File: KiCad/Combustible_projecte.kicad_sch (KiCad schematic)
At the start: 0 parts

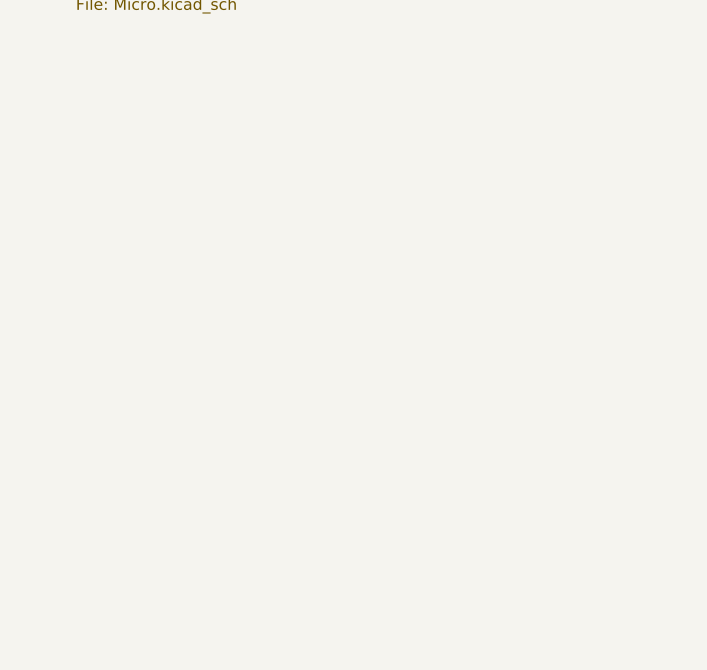
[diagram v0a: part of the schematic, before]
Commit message: Part de potencia acabada, concretar certs pins del micro
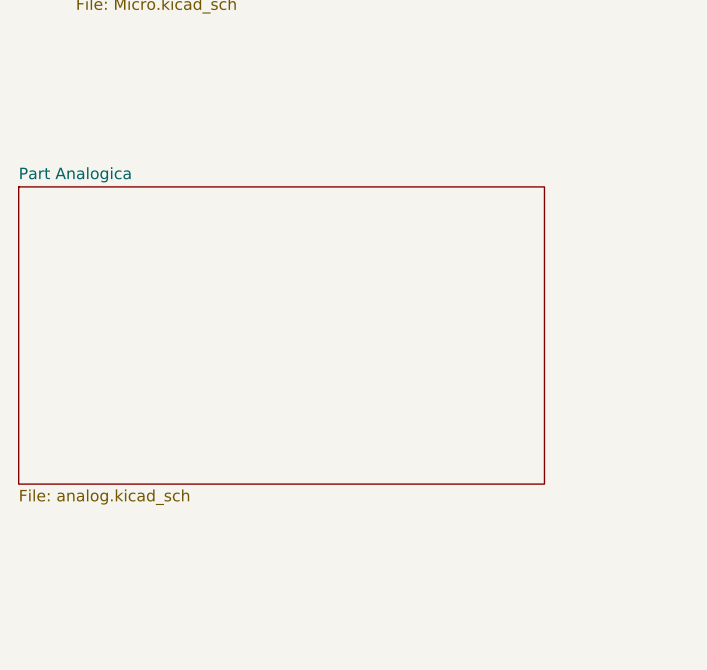
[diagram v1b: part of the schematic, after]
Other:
- added sheet Part Analogica (analog.kicad_sch)
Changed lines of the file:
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@@
+	)
+	(sheet
+		(at 31.75 82.55)
+		(size 58.42 33.02)
+		(exclude_from_sim no)
+		(in_bom yes)
+		(on_board yes)
+		(dnp no)
+		(fields_autoplaced yes)
+		(stroke
+			(width 0.1524)
+			(type solid)
+		)
+		(fill
+			(color 0 0 0 0.0000)
+		)
+		(property "Sheetname" "Part Analogica"
+			(at 31.75 81.8384 0)
+			(effects
+				(font
+					(size 1.27 1.27)
+				)
+				(justify left bottom)
+			)
+		)
+		(property "Sheetfile" "analog.kicad_sch"
+			(at 31.75 116.1546 0)
+			(effects
+				(font
+					(size 1.27 1.27)
+				)
+				(justify left top)
+			)
+		)
+		(instances
+			(project "Combustible_projecte"
+				(path "/c989196d-f442-462e-ad13-2ff17993bc1b"
+					(page "4")
+				)
+			)
+		)
 	)
 	(sheet

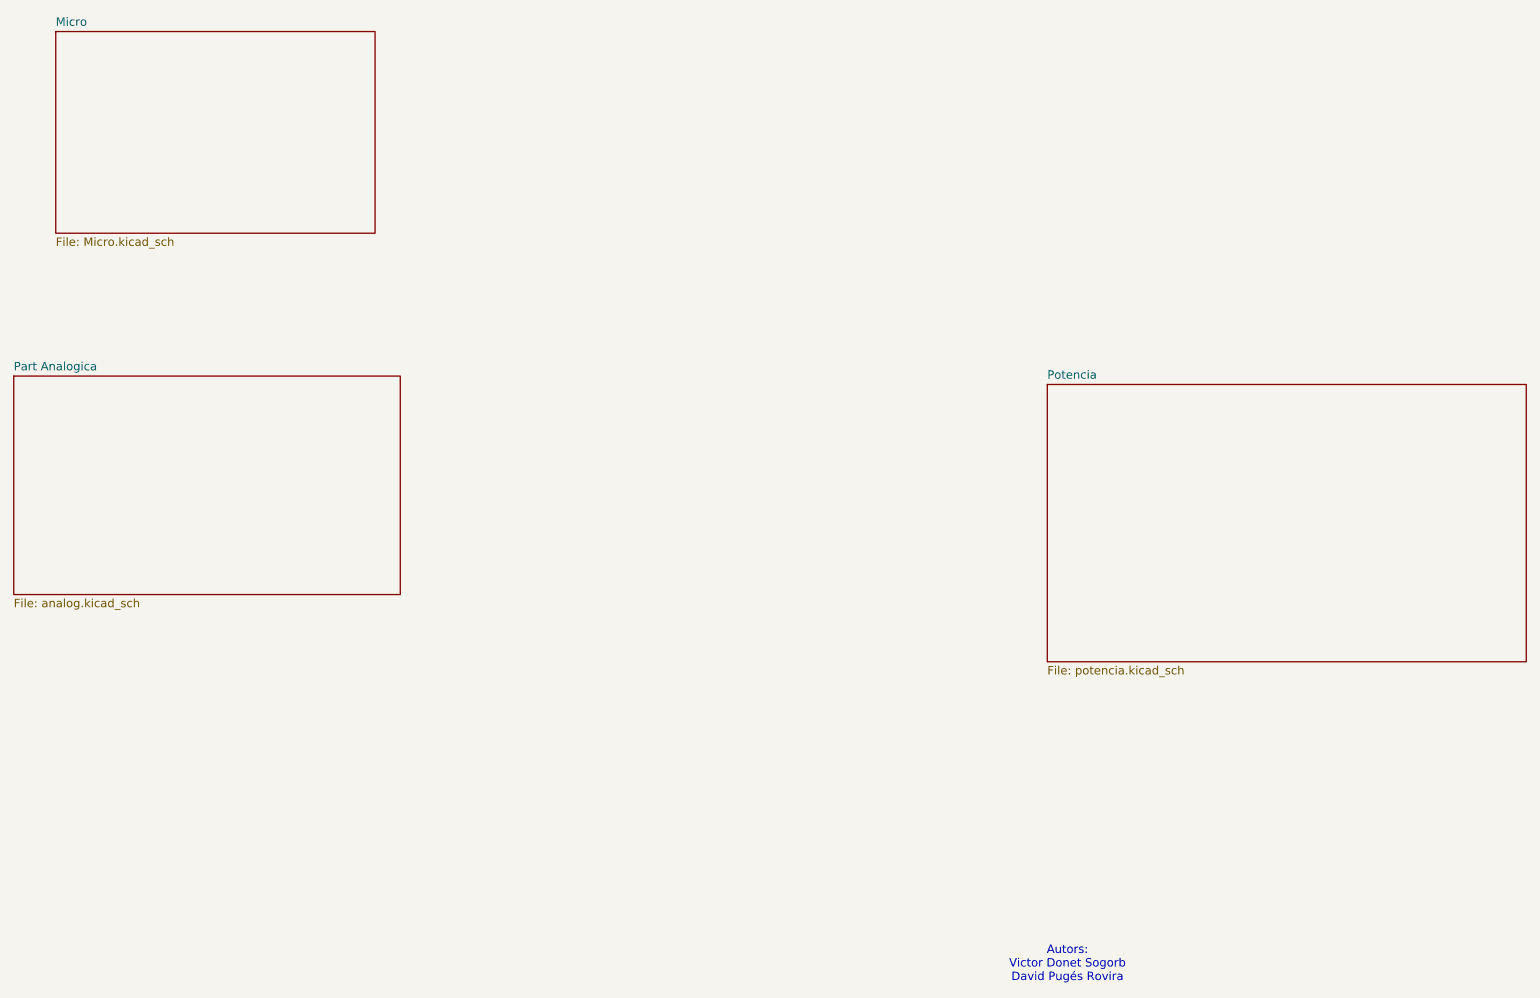
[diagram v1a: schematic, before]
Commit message: Part de potencia moguda al sheet de analogica, esborrat el sheet de potencia
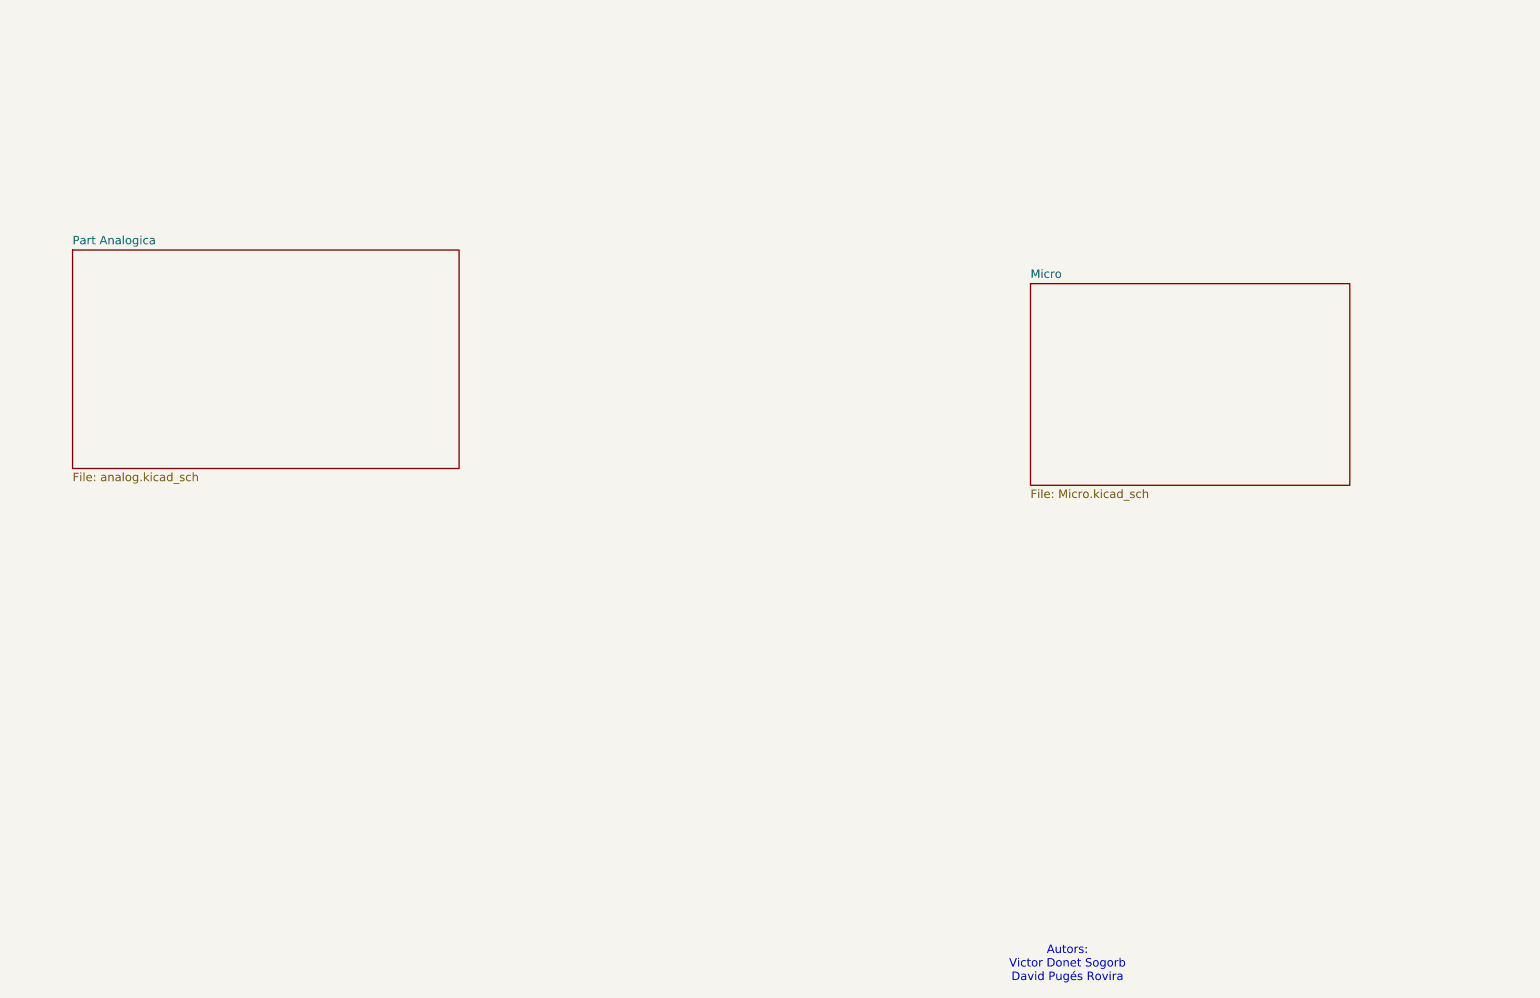
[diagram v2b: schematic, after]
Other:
- removed sheet Potencia
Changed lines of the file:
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@@
 	)
 	(sheet
-		(at 38.1 30.48)
+		(at 185.42 68.58)
 		(size 48.26 30.48)
 		(exclude_from_sim no)
@@
 		)
 		(property "Sheetname" "Micro"
-			(at 38.1 29.7684 0)
+			(at 185.42 67.8684 0)
 			(effects
 				(font
@@
 		)
 		(property "Sheetfile" "Micro.kicad_sch"
-			(at 38.1 61.5446 0)
+			(at 185.42 99.6446 0)
 			(effects
 				(font
@@
 	)
 	(sheet
-		(at 31.75 82.55)
+		(at 40.64 63.5)
 		(size 58.42 33.02)
 		(exclude_from_sim no)
@@
 		)
 		(property "Sheetname" "Part Analogica"
-			(at 31.75 81.8384 0)
+			(at 40.64 62.7884 0)
 			(effects
 				(font
@@
 		)
 		(property "Sheetfile" "analog.kicad_sch"
-			(at 31.75 116.1546 0)
+			(at 40.64 97.1046 0)
 			(effects
 				(font
-					(size 1.27 1.27)
-				)
-				(justify left top)
-			)
-		)
-		(instances
-			(project "Combustible_projecte"
-				(path "/c989196d-f442-462e-ad13-2ff17993bc1b"
-					(page "4")
-				)
-			)
-		)
-	)
-	(sheet
-		(at 187.96 83.82)
-		(size 72.39 41.91)
-		(exclude_from_sim no)
-		(in_bom yes)
-		(on_board yes)
-		(dnp no)
-		(fields_autoplaced yes)
-		(stroke
-			(width 0.1524)
-			(type solid)
-		)
-		(fill
-			(color 0 0 0 0.0000)
-		)
-		(property "Sheetname" "Potencia"
-			(at 187.96 83.1084 0)
-			(effects
-				(font
-					(size 1.27 1.27)
-				)
-				(justify left bottom)
-			)
-		)
-		(property "Sheetfile" "potencia.kicad_sch"
-			(at 187.96 126.3146 0)
-			(effects
-				(font

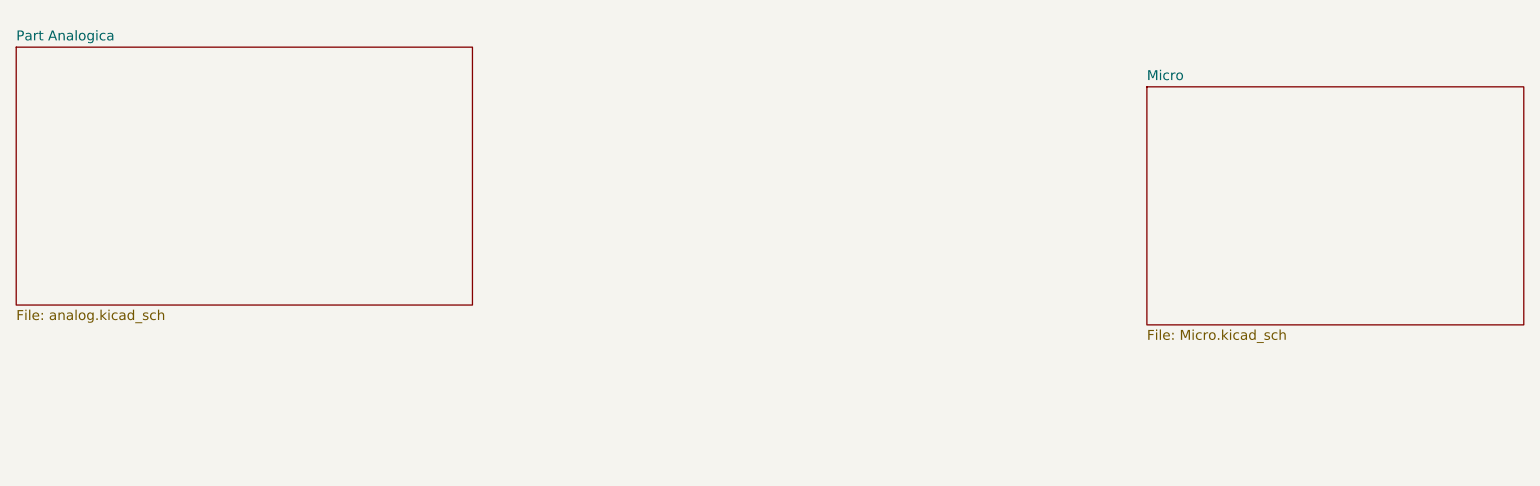
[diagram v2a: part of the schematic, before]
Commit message: Sheets nombrades amb titol, i part del supply millorada
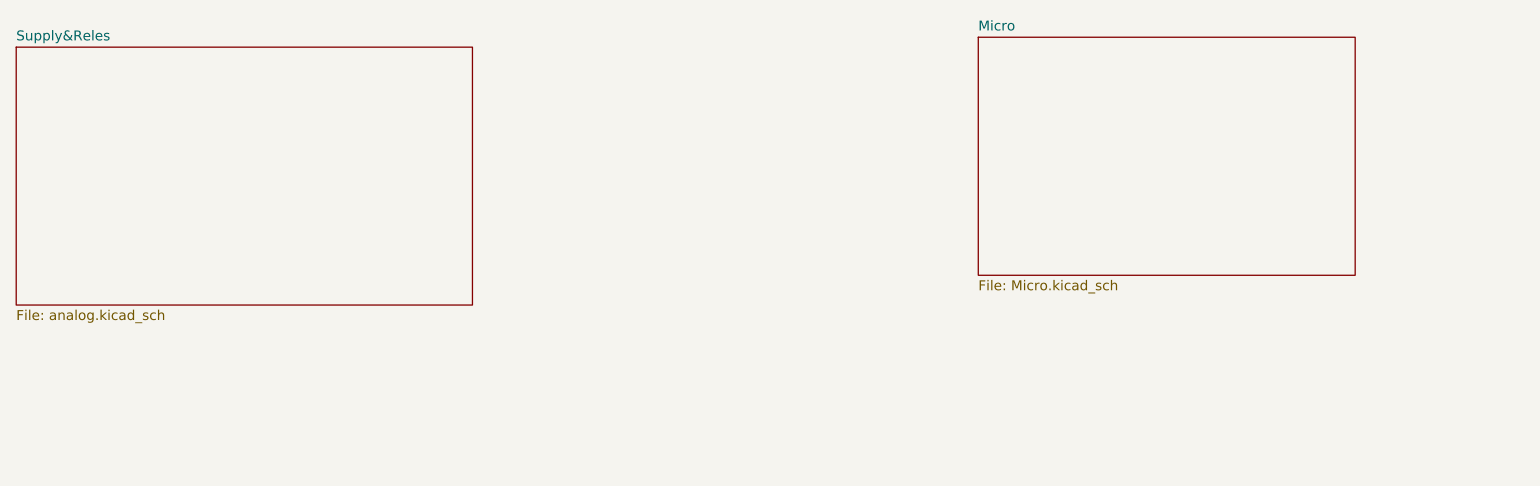
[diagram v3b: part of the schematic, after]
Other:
- sheet Part Analogica renamed Supply&Reles
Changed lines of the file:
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@@
 	)
 	(sheet
-		(at 185.42 68.58)
+		(at 163.83 62.23)
 		(size 48.26 30.48)
 		(exclude_from_sim no)
@@
 		)
 		(property "Sheetname" "Micro"
-			(at 185.42 67.8684 0)
+			(at 163.83 61.5184 0)
 			(effects
 				(font
@@
 		)
 		(property "Sheetfile" "Micro.kicad_sch"
-			(at 185.42 99.6446 0)
+			(at 163.83 93.2946 0)
 			(effects
 				(font
@@
 			(color 0 0 0 0.0000)
 		)
-		(property "Sheetname" "Part Analogica"
+		(property "Sheetname" "Supply&Reles"
 			(at 40.64 62.7884 0)
 			(effects
